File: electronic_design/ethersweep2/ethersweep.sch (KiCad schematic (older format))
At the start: 62 parts, among them J1 AVR-ISP-6, J3 Conn_01x04_Female, J4 Conn_01x02_Male, J5 Conn_01x02_Male, J6 HR911105A, M1 Stepper_Motor_bipolar, SW1 SW_Push, U1 ENC28J60x-SS, U2 ATmega328-AU, U3 DRV8825PWPR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

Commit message: raw component layout done
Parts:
- removed JP1, JP2, JP3: SJ, Jumper:SolderJumper-2_P1.3mm_Open_TrianglePad1.0x1.5mm, symbol Jumper:SolderJumper_2_Open
- added H5, H6, H7, H8: MountingHole_Pad, MountingHole:MountingHole_3.2mm_M3_Pad_Via, symbol Mechanical:MountingHole_Pad
- added J7, J9: Conn_01x04_Female, Connector_PinHeader_2.54mm:PinHeader_1x04_P2.54mm_Vertical, symbol Connector:Conn_01x04_Female
- added J8: AVR-ISP-6, Connector_IDC:IDC-Header_2x03_P2.54mm_Vertical, symbol Connector:AVR-ISP-6
- J2: renamed from J?; footprint (none) -> Connector_AMASS:AMASS_XT60-M_1x02_P7.20mm_Vertical
- RX1, TX1: footprint TestPoint:TestPoint_Pad_D3.0mm -> TestPoint:TestPoint_Pad_D2.0mm
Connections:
- net +3V3: now also J8.2 (VCC)
- net ENDSTOP: now also J7.2 (Pin_2), J9.2 (Pin_2)
- net ESTOP: now also J7.1 (Pin_1), J9.1 (Pin_1)
- net GND: now also H5.1, H6.1, H7.1, H8.1, J8.6 (GND)
- net MISO: now also U1.6 (SO), J8.1 (MISO)
- net MOSI: now also U1.7 (SI), J8.4 (MOSI)
- net SCK: now also U1.8 (SCK), J8.3 (SCK)
- net SCL: now also J7.3 (Pin_3), J9.3 (Pin_3)
- net SDA: now also J7.4 (Pin_4), J9.4 (Pin_4)
- net rst: now also J8.5 (~RST)
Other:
- moved on the sheet: H1, H2, H3, H4, J1

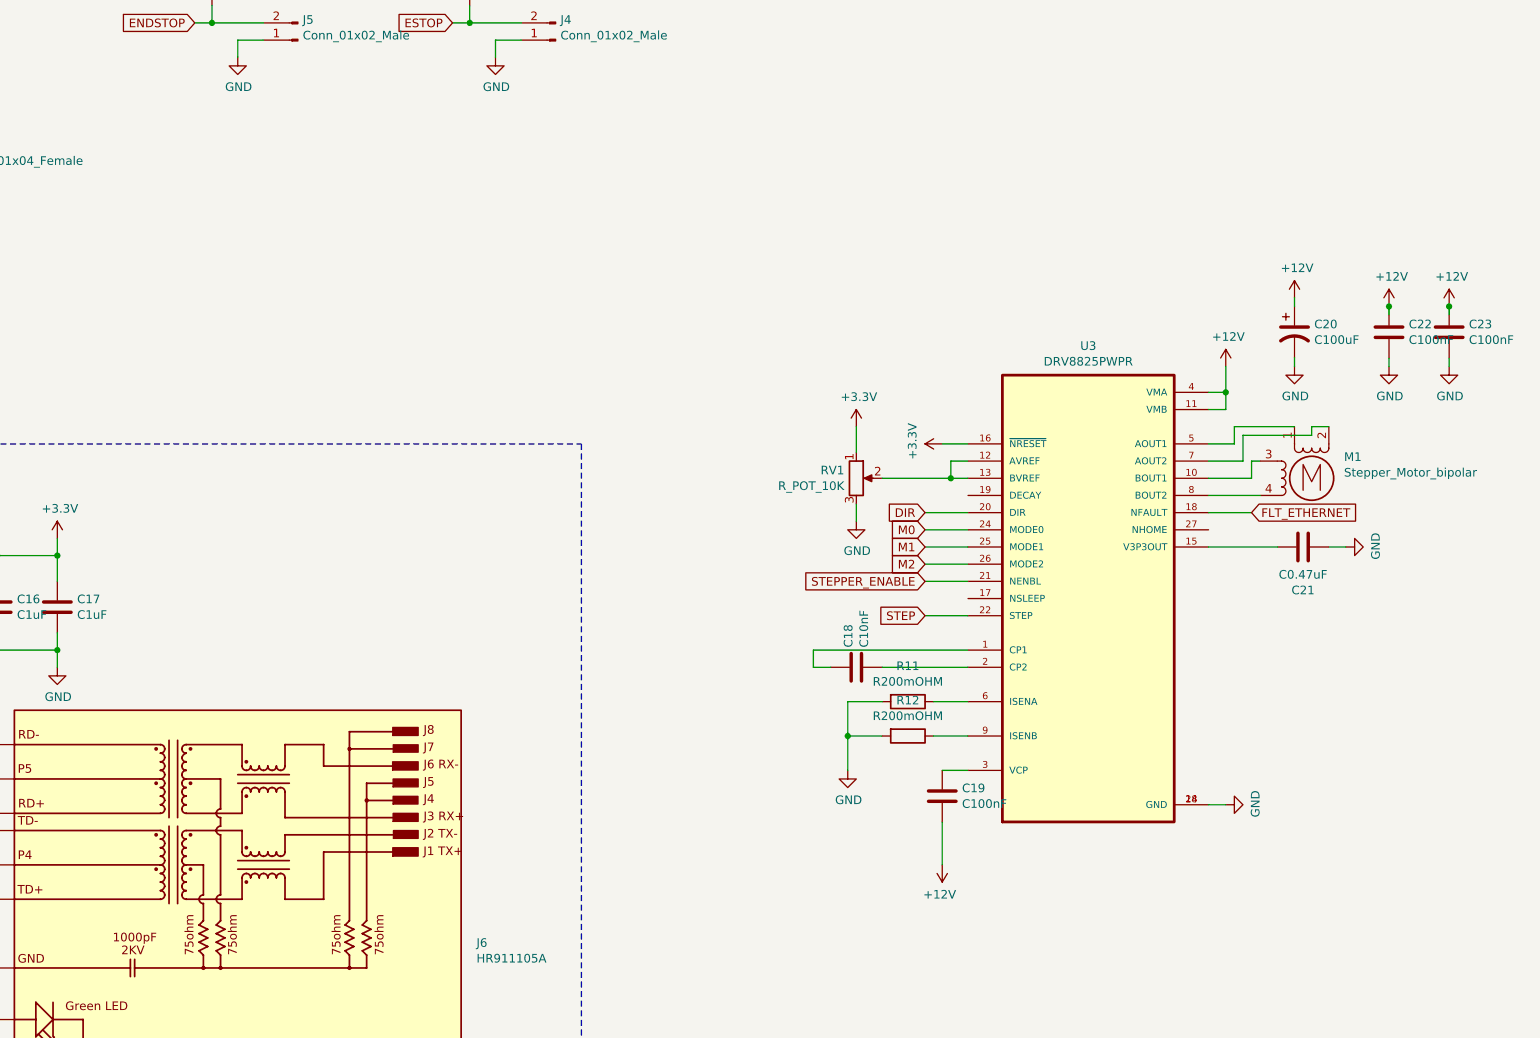
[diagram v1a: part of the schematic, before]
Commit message: board layout and routing for 1st board done
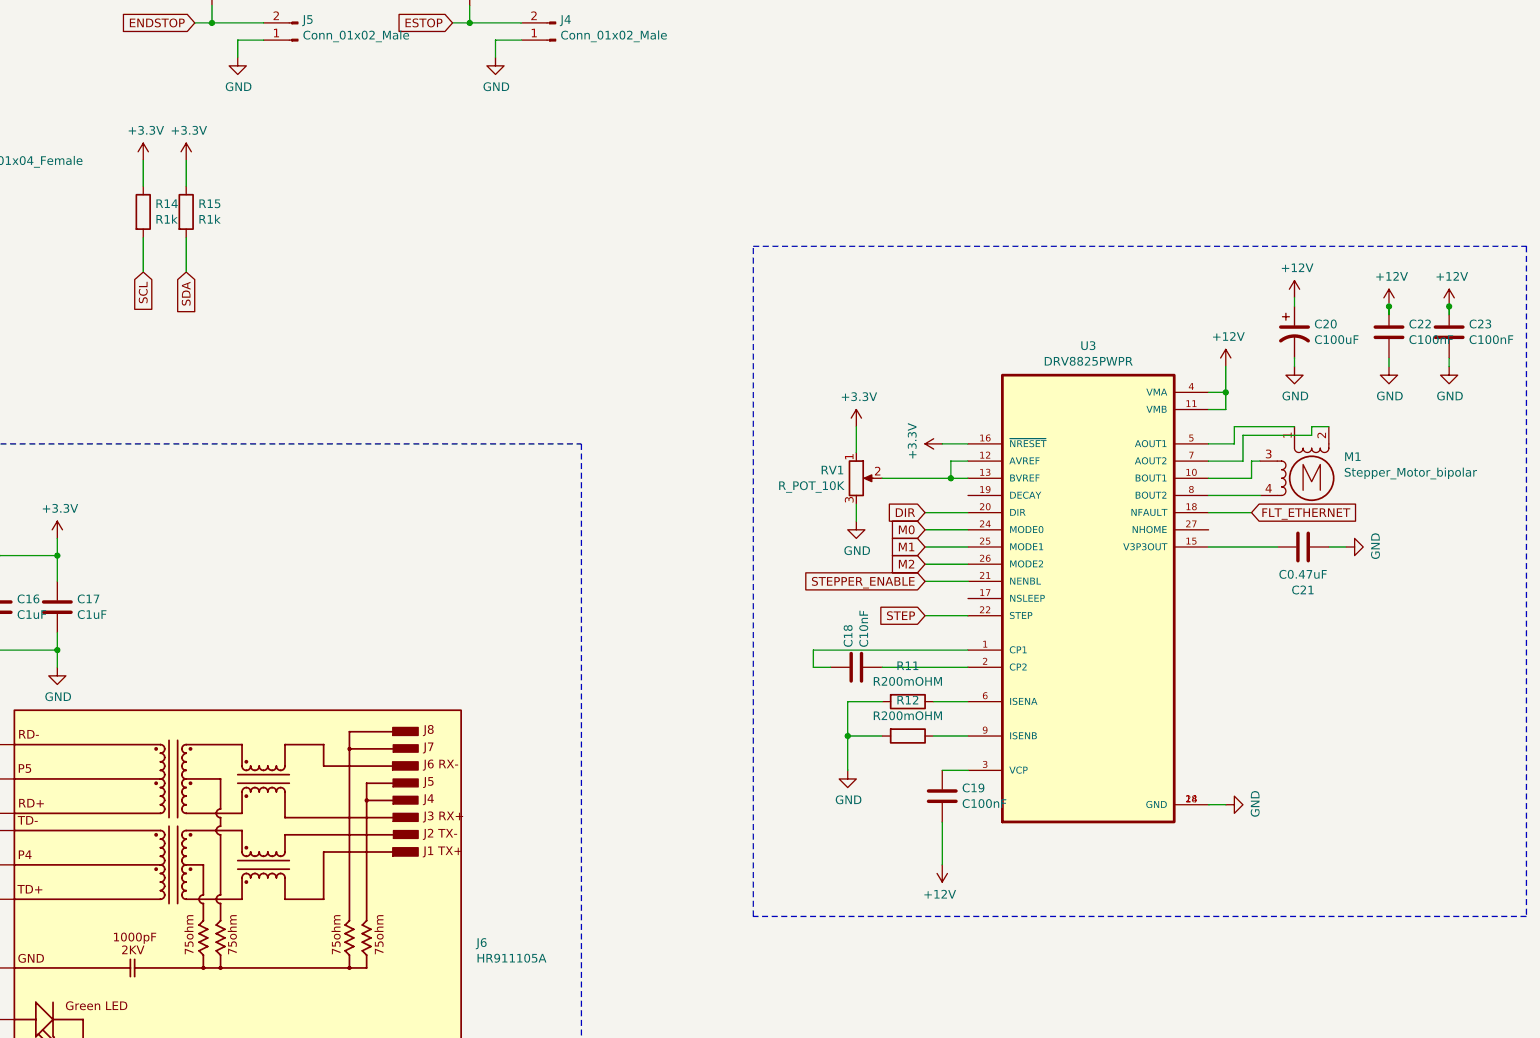
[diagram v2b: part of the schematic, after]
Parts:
- added R14, R15: R1k, Resistor_SMD:R_0603_1608Metric, symbol Device:R
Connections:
- net +3V3: now also R14.1, R15.1
- net SCL: now also R14.2
- net SDA: now also R15.2
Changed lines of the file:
@@
 Wire Wire Line
 	1900 8450 2200 8450
+$Comp
+L Device:R R15
+U 1 1 61BD2D02
+P 8150 4550
+F 0 "R15" H 8220 4596 50  0000 L CNN
+F 1 "R1k" H 8220 4505 50  0000 L CNN
+F 2 "Resistor_SMD:R_0603_1608Metric" V 8080 4550 50  0001 C CNN
+F 3 "~" H 8150 4550 50  0001 C CNN
+	1    8150 4550
+	1    0    0    -1
+$EndComp
+$Comp
+L Device:R R14
+U 1 1 61BD4185
+P 7900 4550
+F 0 "R14" H 7970 4596 50  0000 L CNN
+F 1 "R1k" H 7970 4505 50  0000 L CNN
+F 2 "Resistor_SMD:R_0603_1608Metric" V 7830 4550 50  0001 C CNN
+F 3 "~" H 7900 4550 50  0001 C CNN
+	1    7900 4550
+	1    0    0    -1
+$EndComp
+Text GLabel 8150 4900 3    50   Input ~ 0
+SDA
+Text GLabel 7900 4900 3    50   Input ~ 0
+SCL
+Wire Wire Line
+	7900 4700 7900 4900
+Wire Wire Line
+	8150 4900 8150 4700
+Wire Wire Line
+	7900 4400 7900 4250
+$Comp
+L power:+3.3V #PWR0179
+U 1 1 61C12DB2
+P 7900 4250
+F 0 "#PWR0179" H 7900 4100 50  0001 C CNN
+F 1 "+3.3V" H 7915 4423 50  0000 C CNN
+F 2 "" H 7900 4250 50  0001 C CNN
+F 3 "" H 7900 4250 50  0001 C CNN
+	1    7900 4250
+	1    0    0    -1
+$EndComp
+Wire Wire Line
+	8150 4400 8150 4250
+$Comp
+L power:+3.3V #PWR0180
+U 1 1 61C27BCB
+P 8150 4250
+F 0 "#PWR0180" H 8150 4100 50  0001 C CNN
+F 1 "+3.3V" H 8165 4423 50  0000 C CNN
+F 2 "" H 8150 4250 50  0001 C CNN
+F 3 "" H 8150 4250 50  0001 C CNN
+	1    8150 4250
+	1    0    0    -1
+$EndComp
+Wire Notes Line
+	11450 4750 15950 4750
+Wire Notes Line
+	15950 4750 15950 8650
+Wire Notes Line
+	15950 8650 11450 8650
+Wire Notes Line
+	11450 8650 11450 4750
 $EndSCHEMATC

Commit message: design improvements and error fixes
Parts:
- removed J7, J9: Conn_01x04_Female, Connector_PinHeader_2.54mm:PinHeader_1x04_P2.54mm_Vertical, symbol Connector:Conn_01x04_Female
- added J7: Conn_01x06_Female, Connector_PinHeader_2.54mm:PinHeader_1x06_P2.54mm_Vertical, symbol Connector:Conn_01x06_Female
- added J9: Conn_01x06_Male, Connector_PinHeader_2.54mm:PinHeader_1x06_P2.54mm_Vertical, symbol Connector:Conn_01x06_Male
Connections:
- net SLP_ETHERNET is gone; now on net CS_ETHERNET: U2.14 (PB2)
- net CS_ETHERNET: now also J7.5 (Pin_5), J9.5 (Pin_5); no longer U2.1 (PD3)
- net ENDSTOP: now also U2.1 (PD3), J7.2 (Pin_2), J9.2 (Pin_2); no longer U2.12 (PB0)
- net ESTOP: now also U2.2 (PD4), J7.1 (Pin_1), J9.1 (Pin_1); no longer U2.13 (PB1)
- net RST_ETHERNET: now also U2.13 (PB1), J7.6 (Pin_6), J9.6 (Pin_6); no longer U2.2 (PD4)
- net SCL: now also J7.3 (Pin_3), J9.3 (Pin_3)
- net SDA: now also J7.4 (Pin_4), J9.4 (Pin_4)
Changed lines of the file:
@@
 Wire Wire Line
 	8800 1900 8800 2000
-Text GLabel 2200 1250 2    50   Input ~ 0
+Text GLabel 2200 3250 2    50   Input ~ 0
 ENDSTOP
-Text GLabel 2200 1350 2    50   Input ~ 0
+Text GLabel 2200 3350 2    50   Input ~ 0
 ESTOP
 $Comp
@@
 	1950 1650 2200 1650
 Wire Wire Line
-	1950 1250 2200 1250
-Wire Wire Line
-	2200 1350 1950 1350
+	1950 1350 2200 1350
+Wire Wire Line
+	2200 1450 1950 1450
 $Comp
 L AS5600:AS5600 U5
@@
 Wire Wire Line
 	1350 750  1350 900
-Text GLabel 2200 3250 2    50   Input ~ 0
+Text GLabel 2200 1450 2    50   Input ~ 0
 CS_ETHERNET
 Wire Wire Line
 	1950 3250 2200 3250
-Text GLabel 2200 3350 2    50   Input ~ 0
+Text GLabel 2200 1350 2    50   Input ~ 0
 RST_ETHERNET
 Wire Wire Line
@@
 Wire Wire Line
 	1950 2450 2200 2450
-Text GLabel 2200 1450 2    50   Input ~ 0
-SLP_ETHERNET
-Wire Wire Line
-	1950 1450 2200 1450
 $Comp
 L MCU_Microchip_ATmega:ATmega328-AU U2
@@
 $EndComp
 $Comp
-L Connector:Conn_01x04_Female J7
-U 1 1 618AEEEB
-P 6550 4100
-F 0 "J7" V 6488 3812 50  0000 R CNN
-F 1 "Conn_01x04_Female" V 6397 3812 50  0000 R CNN
-F 2 "Connector_PinHeader_2.54mm:PinHeader_1x04_P2.54mm_Vertical" H 6550 4100 50  0001 C CNN
-F 3 "~" H 6550 4100 50  0001 C CNN
-	1    6550 4100
-	0    -1   -1   0
-$EndComp
-Text GLabel 6750 4500 3    50   Input ~ 0
-SDA
-Text GLabel 6650 4500 3    50   Input ~ 0
-SCL
-Wire Wire Line
-	6650 4300 6650 4500
-Wire Wire Line
-	6750 4500 6750 4300
-Wire Wire Line
-	6550 4400 6550 4300
-Text GLabel 6550 4400 3    50   Input ~ 0
-ENDSTOP
-Wire Wire Line
-	6450 4400 6450 4300
-Text GLabel 6450 4400 3    50   Input ~ 0
-ESTOP
-$Comp
 L Mechanical:MountingHole_Pad H8
 U 1 1 6192C950
@@
 Wire Wire Line
 	4200 1700 4200 1800
-$Comp
-L Connector:Conn_01x04_Female J9
-U 1 1 61992053
-P 6050 4100
-F 0 "J9" V 5988 3812 50  0000 R CNN
-F 1 "Conn_01x04_Female" V 5897 3812 50  0000 R CNN
-F 2 "Connector_PinHeader_2.54mm:PinHeader_1x04_P2.54mm_Vertical" H 6050 4100 50  0001 C CNN
-F 3 "~" H 6050 4100 50  0001 C CNN
-	1    6050 4100
-	0    -1   -1   0
-$EndComp
-Text GLabel 6250 4500 3    50   Input ~ 0
+Text GLabel 5850 4550 3    50   Input ~ 0
 SDA
-Text GLabel 6150 4500 3    50   Input ~ 0
+Text GLabel 5750 4550 3    50   Input ~ 0
 SCL
 Wire Wire Line
-	6150 4300 6150 4500
-Wire Wire Line
-	6250 4500 6250 4300
-Wire Wire Line
-	6050 4400 6050 4300
-Text GLabel 6050 4400 3    50   Input ~ 0
+	5750 4350 5750 4550
+Wire Wire Line
+	5850 4550 5850 4350
+Wire Wire Line
+	5650 4450 5650 4350
+Text GLabel 5650 4450 3    50   Input ~ 0
 ENDSTOP
 Wire Wire Line
-	5950 4400 5950 4300
-Text GLabel 5950 4400 3    50   Input ~ 0
+	5550 4450 5550 4350
+Text GLabel 5550 4450 3    50   Input ~ 0
 ESTOP
 Wire Wire Line
@@
 Wire Notes Line
 	11450 8650 11450 4750
+Text GLabel 6050 4550 3    50   Input ~ 0
+RST_ETHERNET
+Text GLabel 5950 4550 3    50   Input ~ 0
+CS_ETHERNET
+$Comp
+L Connector:Conn_01x06_Female J7
+U 1 1 61DB5EEA
+P 5750 4150
+F 0 "J7" V 5688 3762 50  0000 R CNN
+F 1 "Conn_01x06_Female" V 5597 3762 50  0000 R CNN
+F 2 "Connector_PinHeader_2.54mm:PinHeader_1x06_P2.54mm_Vertical" H 5750 4150 50  0001 C CNN
+F 3 "~" H 5750 4150 50  0001 C CNN
+	1    5750 4150
+	0    -1   -1   0
+$EndComp
+$Comp
+L Connector:Conn_01x06_Male J9
+U 1 1 61DB8F12
+P 6700 4150
+F 0 "J9" V 6762 4394 50  0000 L CNN
+F 1 "Conn_01x06_Male" V 6853 4394 50  0000 L CNN
+F 2 "Connector_PinHeader_2.54mm:PinHeader_1x06_P2.54mm_Vertical" H 6700 4150 50  0001 C CNN
+F 3 "~" H 6700 4150 50  0001 C CNN
+	1    6700 4150
+	0    1    1    0
+$EndComp
+Wire Wire Line
+	5950 4550 5950 4350
+Wire Wire Line
+	6050 4550 6050 4350
+Text GLabel 6600 4550 3    50   Input ~ 0
+SDA
+Text GLabel 6700 4550 3    50   Input ~ 0
+SCL
+Wire Wire Line
+	6700 4350 6700 4550
+Wire Wire Line
+	6600 4550 6600 4350
+Wire Wire Line
+	6800 4450 6800 4350
+Text GLabel 6800 4450 3    50   Input ~ 0
+ENDSTOP
+Wire Wire Line
+	6900 4450 6900 4350
+Text GLabel 6900 4450 3    50   Input ~ 0
+ESTOP
+Text GLabel 6400 4550 3    50   Input ~ 0
+RST_ETHERNET
+Text GLabel 6500 4550 3    50   Input ~ 0
+CS_ETHERNET
+Wire Wire Line
+	6500 4550 6500 4350
+Wire Wire Line
+	6400 4550 6400 4350
 $EndSCHEMATC

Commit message: added prod files
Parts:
- R1, R2: value R5k -> R10k; footprint Resistor_SMD:R_0805_2012Metric -> Resistor_SMD:R_0603_1608Metric
- R3: footprint Resistor_SMD:R_0805_2012Metric -> Resistor_SMD:R_0603_1608Metric
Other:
- moved on the sheet: C1, C10, C8, RX1, TX1, U2, Y2

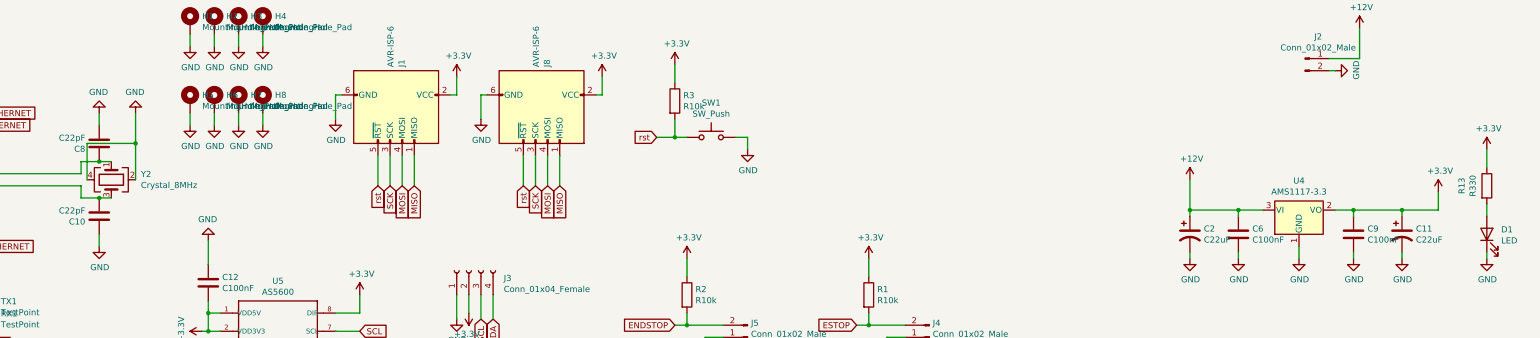
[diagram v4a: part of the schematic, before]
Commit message: added LCSC part numbers and changed some components for cheap manufacturing
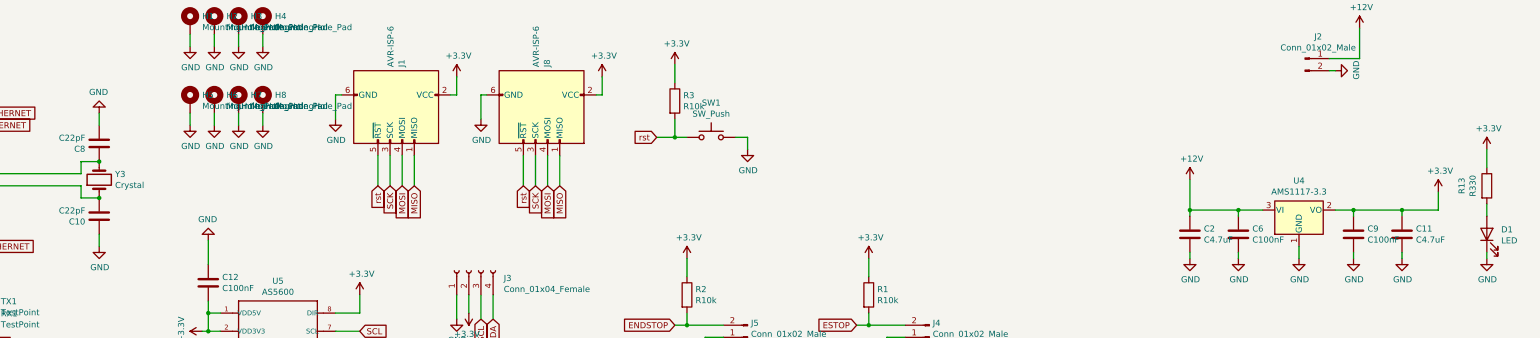
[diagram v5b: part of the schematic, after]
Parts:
- removed C11, C2: C22uF, Capacitor_Tantalum_SMD:CP_EIA-3216-12_Kemet-S, symbol Device:CP1
- removed Y2: Crystal_8MHz, Crystal:Crystal_SMD_3225-4Pin_3.2x2.5mm, symbol Device:Crystal_GND24
- added C11, C2: C4.7uF, Capacitor_SMD:C_1206_3216Metric, symbol Device:C
- added Y3: Crystal, Crystal:Crystal_SMD_5032-2Pin_5.0x3.2mm, symbol Device:Crystal
- C1, C12, C19, C22, C23, C6, C9: LCSC (none) -> C49678
- C10, C4, C5, C8: LCSC (none) -> C1555
- C13, C14, C15, C16, C17, C3, C7: LCSC (none) -> C28323
- C18: LCSC (none) -> C1710
- C20: LCSC (none) -> C176665
- C21: LCSC (none) -> C13967
- D1: LCSC (none) -> C84256
- J6: LCSC (none) -> C12074
- R1, R2, R3: LCSC (none) -> C25804
- R10, R14, R15, R4, R7, R8, R9: LCSC (none) -> C21190
- R11, R12: LCSC (none) -> C25335
- R13: LCSC (none) -> C23138
- RV1: LCSC (none) -> C118954
- U2: LCSC (none) -> C14877
- U3: LCSC (none) -> C81582
- U4: LCSC (none) -> C6186
- Y1: LCSC (none) -> C9006
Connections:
- net +12V: now also C2.1
- net +3V3: now also C11.1
- net GND: now also C11.2, C2.2
- net at C8.1, U2.7 (XTAL1/PB6): now also Y3.2
- net at C10.2, U2.8 (XTAL2/PB7): now also Y3.1

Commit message: cleanup
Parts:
- added TP1, TP2: TestPoint, TestPoint:TestPoint_Pad_D2.0mm, symbol Connector:TestPoint
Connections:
- net +3V3: now also TP1.1
- net GND: now also TP2.1
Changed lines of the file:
@@
 	1    0    0    -1
 $EndComp
+$Comp
+L Connector:TestPoint TP1
+U 1 1 603FD0AE
+P 3900 4500
+F 0 "TP1" H 3958 4618 50  0000 L CNN
+F 1 "TestPoint" H 3958 4527 50  0000 L CNN
+F 2 "TestPoint:TestPoint_Pad_D2.0mm" H 4100 4500 50  0001 C CNN
+F 3 "~" H 4100 4500 50  0001 C CNN
+	1    3900 4500
+	0    1    1    0
+$EndComp
+$Comp
+L Connector:TestPoint TP2
+U 1 1 603FE9A9
+P 3900 4600
+F 0 "TP2" H 3958 4718 50  0000 L CNN
+F 1 "TestPoint" H 3958 4627 50  0000 L CNN
+F 2 "TestPoint:TestPoint_Pad_D2.0mm" H 4100 4600 50  0001 C CNN
+F 3 "~" H 4100 4600 50  0001 C CNN
+	1    3900 4600
+	0    1    1    0
+$EndComp
+$Comp
+L power:GND #PWR0143
+U 1 1 6043D76B
+P 3700 4600
+F 0 "#PWR0143" H 3700 4350 50  0001 C CNN
+F 1 "GND" H 3705 4427 50  0000 C CNN
+F 2 "" H 3700 4600 50  0001 C CNN
+F 3 "" H 3700 4600 50  0001 C CNN
+	1    3700 4600
+	0    1    1    0
+$EndComp
+Wire Wire Line
+	3900 4600 3700 4600
+Wire Wire Line
+	3900 4500 3750 4500
+$Comp
+L power:+3.3V #PWR0181
+U 1 1 60452E8B
+P 3750 4500
+F 0 "#PWR0181" H 3750 4350 50  0001 C CNN
+F 1 "+3.3V" H 3765 4673 50  0000 C CNN
+F 2 "" H 3750 4500 50  0001 C CNN
+F 3 "" H 3750 4500 50  0001 C CNN
+	1    3750 4500
+	0    -1   -1   0
+$EndComp
 $EndSCHEMATC

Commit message: added production files, BOM and POS files with JLCPCB part numbers and orientations
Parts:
- R5, R6: LCSC (none) -> C23138
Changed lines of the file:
@@
 F 2 "Resistor_SMD:R_0603_1608Metric" V 3930 8150 50  0001 C CNN
 F 3 "~" H 4000 8150 50  0001 C CNN
+F 4 "C23138" V 4000 8150 50  0001 C CNN "LCSC"
 	1    4000 8150
 	0    1    1    0
@@
 F 2 "Resistor_SMD:R_0603_1608Metric" V 3930 8250 50  0001 C CNN
 F 3 "~" H 4000 8250 50  0001 C CNN
+F 4 "C23138" V 4000 8250 50  0001 C CNN "LCSC"
 	1    4000 8250
 	0    1    1    0
